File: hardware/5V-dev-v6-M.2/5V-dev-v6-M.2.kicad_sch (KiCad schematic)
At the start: 75 parts, among them J1 USB_B_Micro - 10118193-0001LF, J10 Conn_01x02_Male, J11 Conn_01x20_Female, J12 Conn_01x27_Female, J13 Conn_01x02_Male, J2 Conn_01x02_Female, J3 Conn_01x02_Male, J4 Conn_01x03_Female, J5 Conn_01x02_Male, J6 Conn_01x02_Male, J7 Conn_01x06_Female, J8 Conn_01x02_Male, J9 Conn_01x02_Male, SW1 SW_Push - SKQGADE010, T1 Logo, T2 Logo, U1 FT232H, U10 TXB0104PWR, U2 SN74LVC1G125DCKR, U3 SN74LVC1G125DCKR, U4 MCP1319MT-29LE-OT, U5 TAR5SxxU_SOT353F, U6 TXB0104PWR, U7 W25Q32FVSS, U8 caravel-M.2-card, U9 TXB0104PWR, X1 SG7050CCN_10MHZ, Y1 CSTNE12M0GH5L000R0

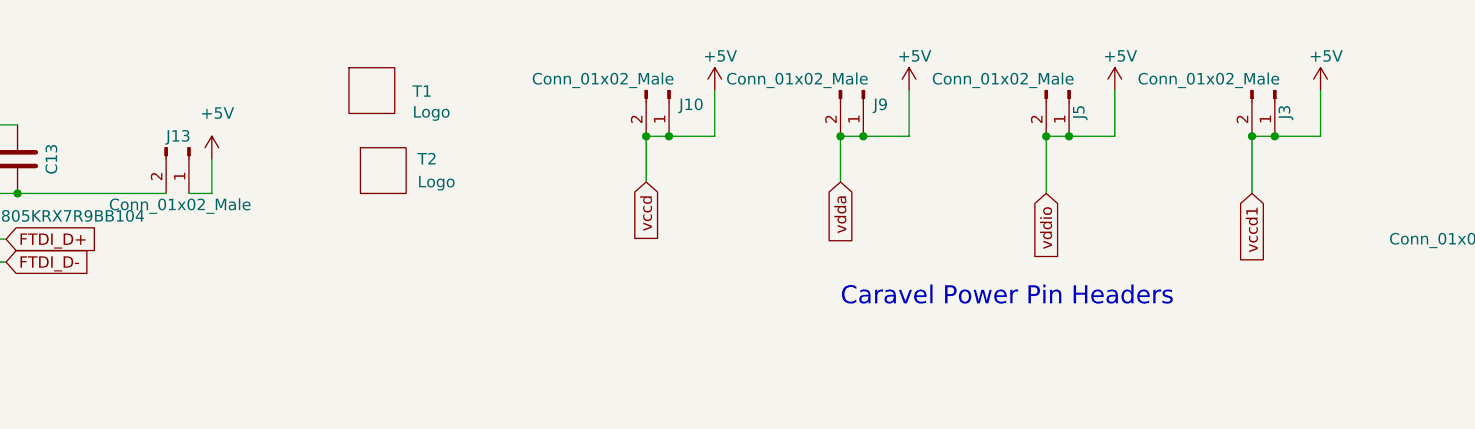
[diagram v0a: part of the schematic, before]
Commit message: add 5V development board (REV 6A) PCB and gerbers
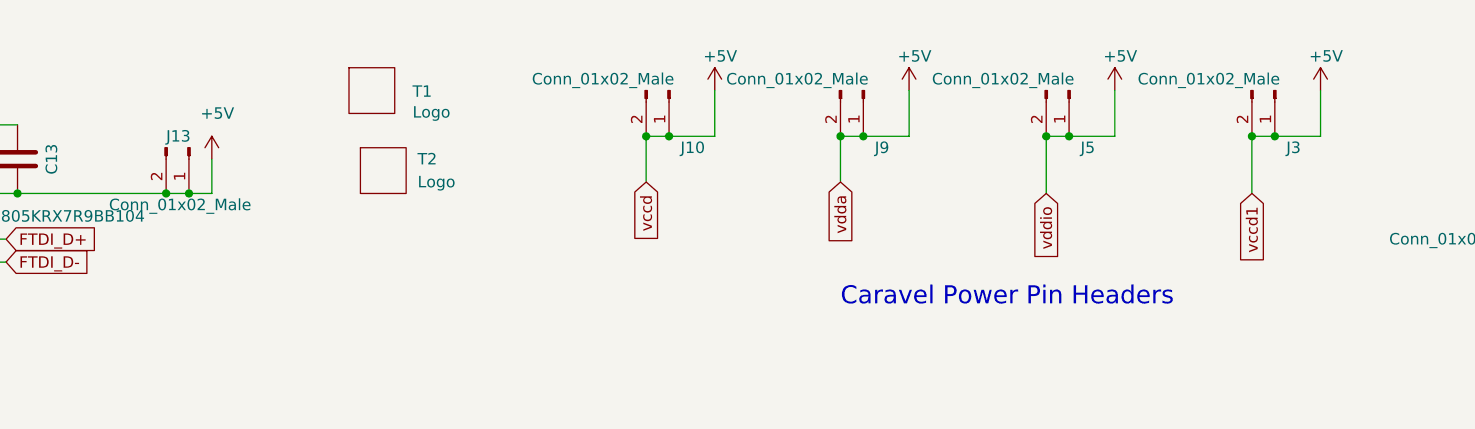
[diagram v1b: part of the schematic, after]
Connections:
- net +5V: now also C13.1, C14.2, J1.1 (VBUS), J13.2 (Pin_2)
